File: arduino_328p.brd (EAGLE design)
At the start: 50.8 x 36.8 mm, 15 parts, among them J2 AVR_SPI_PROG_3X2PTH, J3 6_PIN_SERIAL_CABLEPTH, J5 POWER_JACK, U1 328P

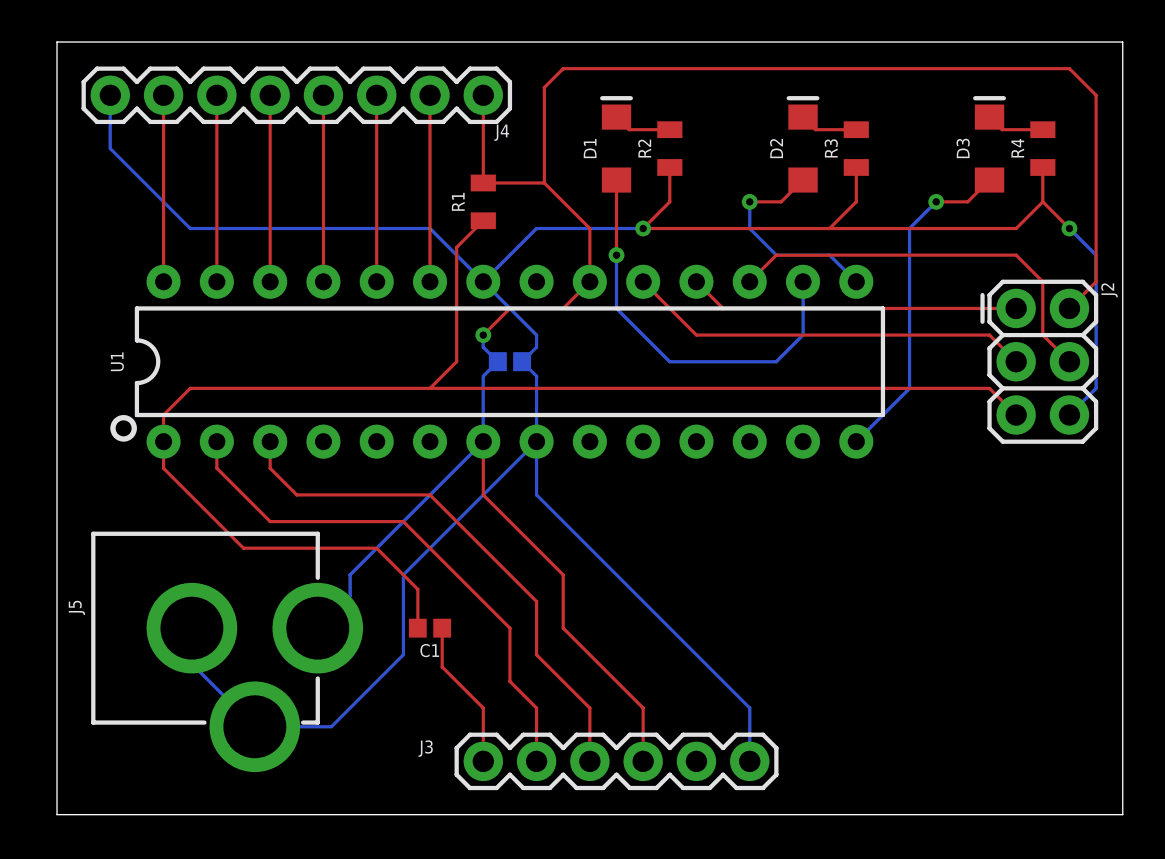
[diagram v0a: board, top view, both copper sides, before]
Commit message: copper pours and sikscreen
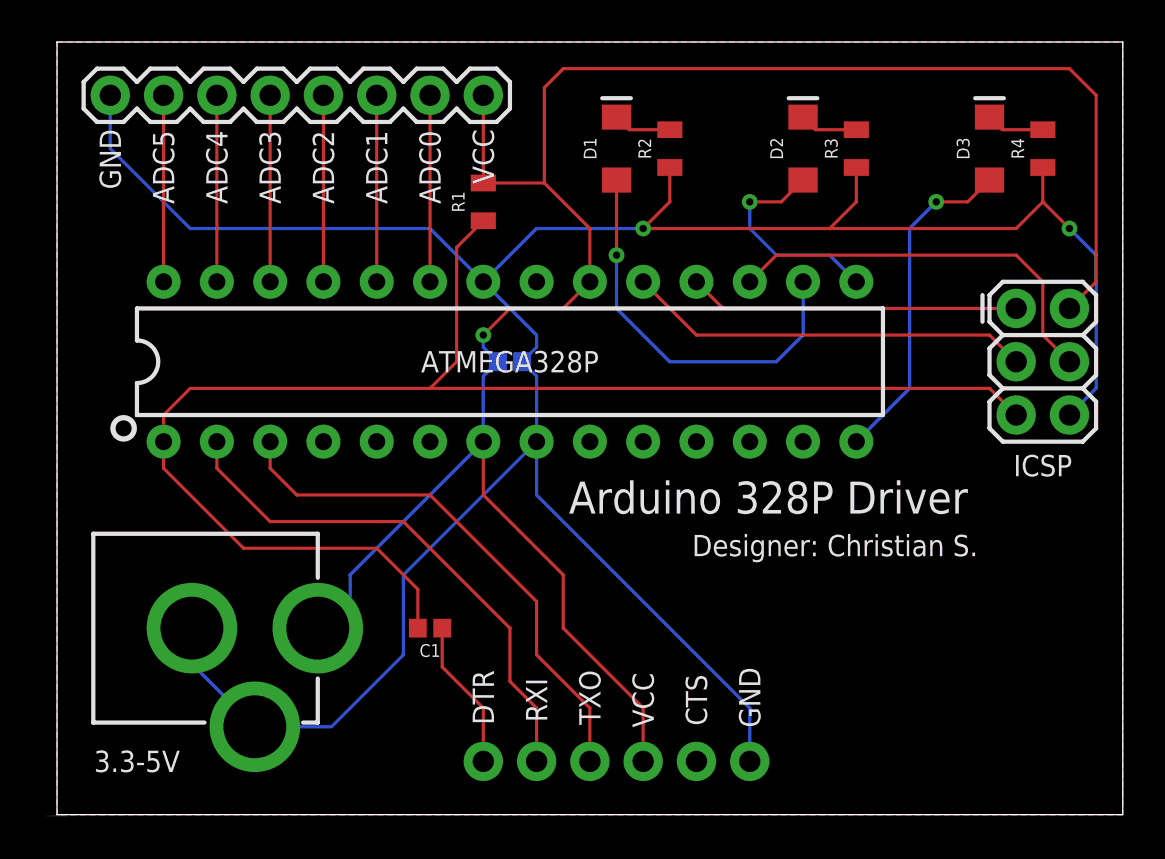
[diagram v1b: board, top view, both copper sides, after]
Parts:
- removed FRAME1: FRAME-LETTER, SparkFun-Aesthetics:CREATIVE_COMMONS
- removed J3: 6_PIN_SERIAL_CABLEPTH, SparkFun-Connectors:FTDI_BASIC
- added J1: (no value), SparkFun-Connectors:1X06-KIT
- R1: value 0.22 -> 1K
- R2, R3: value 0.22 -> 330
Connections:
- net CTS: now also J1.5; no longer J3.CTS
- net DTR: now also J1.1; no longer J3.DTR
- net GND: now also J1.6; no longer J3.GND
- net RX: now also J1.2; no longer J3.RXI
- net TX: now also J1.3; no longer J3.TXO
- net VCC: now also J1.4; no longer J3.VCC
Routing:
- added copper zone on layer 1, net GND
- added copper zone on layer 16, net GND
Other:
- board text added: "/home/christian/Documents/open-herb/media/icon-transparent.bmp"
- board text added: "3.3-5V"
- board text added: "ADC0"
- board text added: "ADC1"
- board text added: "ADC2"
- board text added: "ADC3"
- board text added: "ADC4"
- board text added: "ADC5"
- board text added: "ATMEGA328P"
- board text added: "Arduino 328P Driver"
- board text added: "CTS"
- board text added: "DTR"
- board text added: "Designer: Christian S."
- board text added: "GND"
- board text added: "ICSP"
- board text added: "RXI"
- board text added: "TXO"
- board text added: "VCC"

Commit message: change current limit resistor to 330
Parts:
- R4: value 0.22 -> 330
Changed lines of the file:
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@@
 <attribute name="VALUE" x="38.989" y="31.75" size="0.6096" layer="27" font="vector" ratio="20" rot="R90" align="top-center"/>
 </element>
-<element name="R4" library="SparkFun-Resistors" package="0805" value="0.22" x="46.99" y="31.75" smashed="yes" rot="R90">
+<element name="R4" library="SparkFun-Resistors" package="0805" value="330" x="46.99" y="31.75" smashed="yes" rot="R90">
 <attribute name="NAME" x="46.101" y="31.75" size="0.6096" layer="25" font="vector" ratio="20" rot="R90" align="bottom-center"/>
 <attribute name="PROD_ID" value="RES-09883" x="95.25" y="86.36" size="1.778" layer="27" rot="R90" display="off"/>
